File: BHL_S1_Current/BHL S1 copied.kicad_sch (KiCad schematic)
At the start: 96 parts, among them J1 Conn_01x03_Pin, J2 Conn_01x03_Pin, Q1 CSD19502Q5B, Q2 CSD19502Q5B, Q3 CSD19502Q5B, Q4 CSD19502Q5B, Q5 CSD19502Q5B, Q6 CSD19502Q5B, SW1 SW_Push, U1 ME6211C30M5, U2 SPX3819M5-L-5-0, U3 Solder Pad, U4 STM32G431CBUx, Y2 8MHz

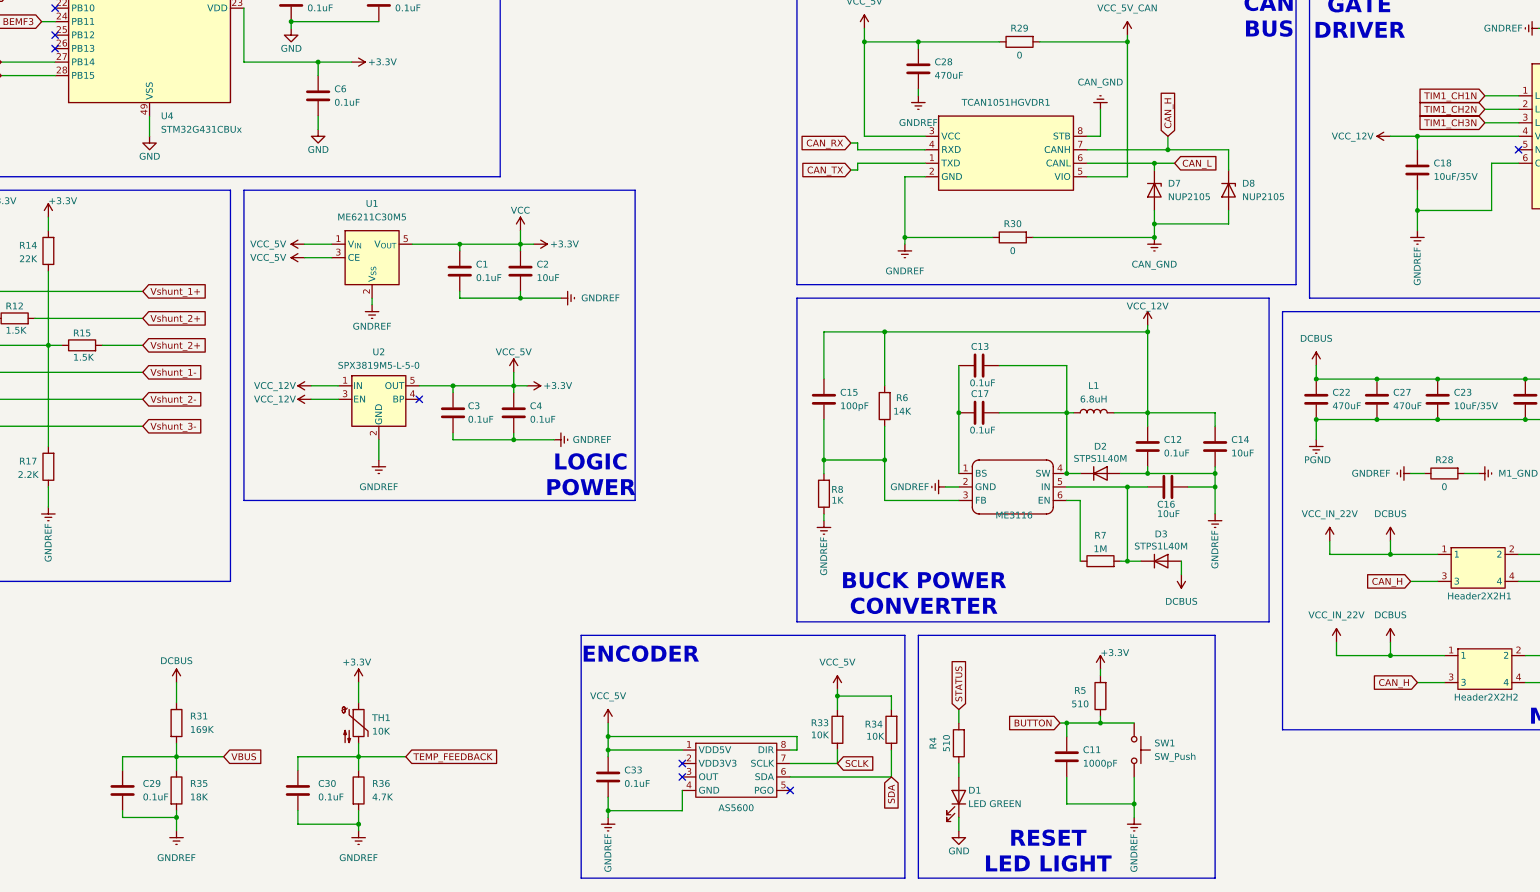
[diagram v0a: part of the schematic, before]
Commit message: Cleanup, Organization, and some edits
Editing the schematic and the PCB. Fixed a lot of ERC errors. Organized the mess that it originally was.
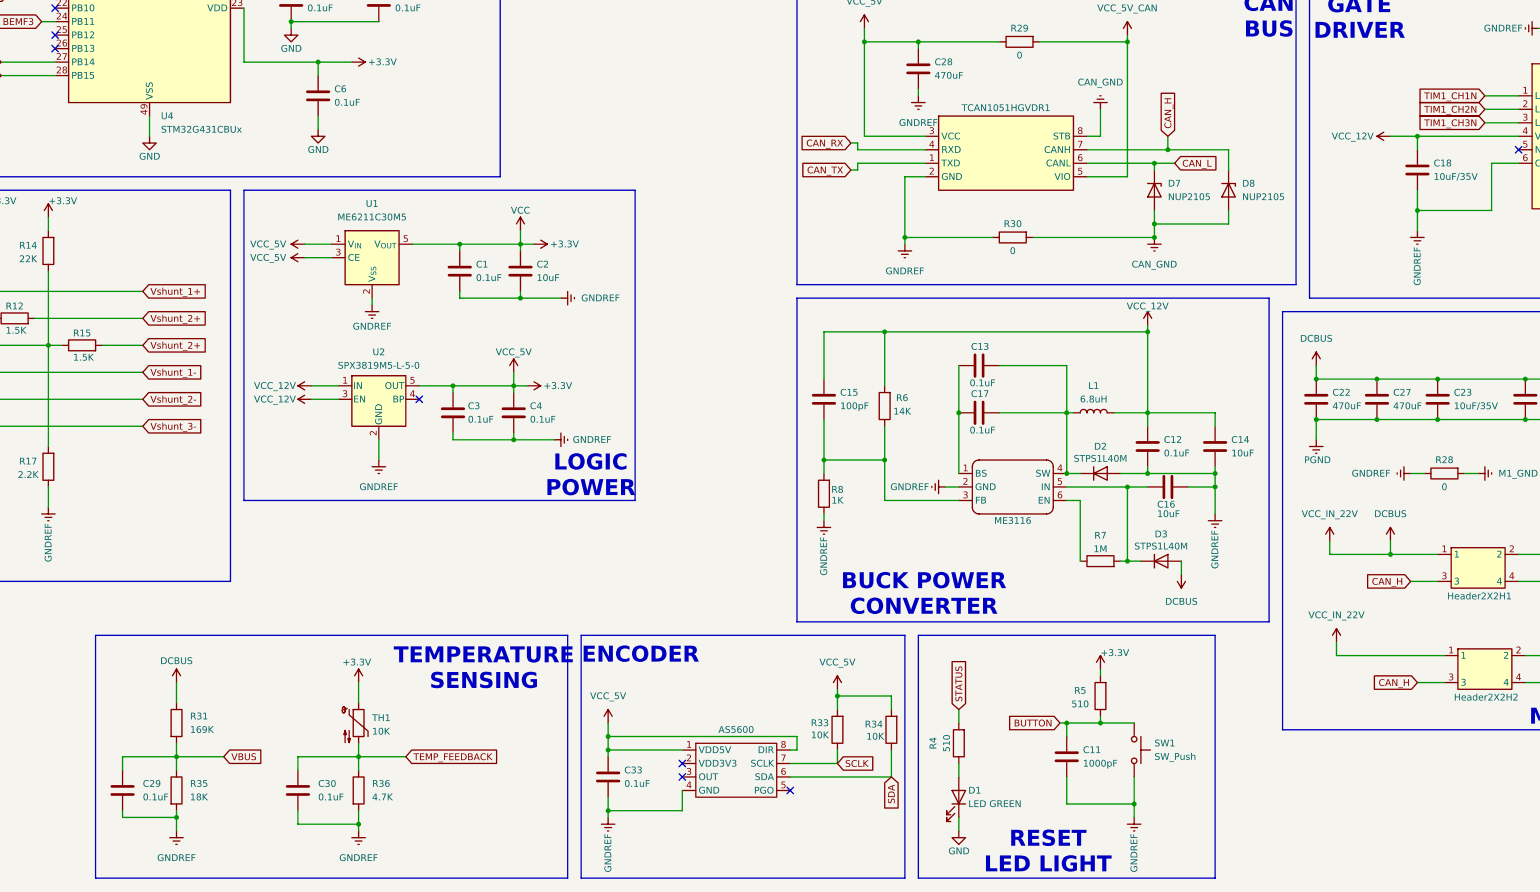
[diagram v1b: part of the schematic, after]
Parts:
- AS5600: symbol Buck converter:AS5600 -> BHL_S1_Components:AS5600
- Header2X2H1, Header2X2H2: symbol Buck converter:Header_2X2H -> BHL_S1_Components:Header_2X2H
- IR2136STRPBF1: symbol Buck converter:IR2136STRPBF -> BHL_S1_Components:IR2136STRPBF
- ME3116: symbol Buck converter:ME3116 -> BHL_S1_Components:ME3116
- TCAN1051HGVDR1: symbol Buck converter:TCAN1051HGVDR -> BHL_S1_Components:TCAN1051HGVDR
- U3: symbol Buck converter:SOLDERPAD_BLDC -> BHL_S1_Components:SOLDERPAD_BLDC
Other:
- note added: "TEMPERATURE SENSING"
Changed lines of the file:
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@@
 	)
 	(rectangle
+		(start 86.36 233.68)
+		(end 175.26 279.4)
+		(stroke
+			(width 0)
+			(type default)
+		)
+		(fill
+			(type none)
+		)
+	)
+	(rectangle
 		(start 241.3 233.68)
 		(end 297.18 279.4)
@@
 		)
 	)
+	(text "TEMPERATURE \nSENSING"
+		(exclude_from_sim no)
+		(at 159.512 240.03 0)
+		(effects
+			(font
+				(face "KiCad Font")
+				(size 3 3)
+				(thickness 2)
+				(bold yes)
+				(color 194 0 0 1)
+			)
+		)
+	)
 	(text "LOGIC\nPOWER\n"
 		(exclude_from_sim no)
@@
 	)
 	(junction
-		(at 330.2 237.49)
-		(diameter 0)
-		(color 0 0 0 0)
-	)
-	(junction
 		(at 223.52 200.66)
 		(diameter 0)
@@
 	(wire
 		(pts
-			(xy 330.2 234.95) (xy 330.2 237.49)
-		)
-		(stroke
-			(width 0)
-			(type default)
-		)
-	)
-	(wire
-		(pts
 			(xy 361.95 88.9) (xy 364.49 88.9)
 		)
@@
 	(wire
 		(pts
-			(xy 340.36 237.49) (xy 330.2 237.49)
+			(xy 320.04 237.49) (xy 340.36 237.49)
 		)
 		(stroke
@@
 	(wire
 		(pts
-			(xy 330.2 237.49) (xy 320.04 237.49)
-		)
-		(stroke
-			(width 0)
-			(type default)
-		)
-	)
-	(wire
-		(pts
 			(xy 375.92 99.06) (xy 375.92 104.14)
 		)
@@
 	)
 	(symbol
-		(lib_id "Buck converter:Header_2X2H")
+		(lib_id "BHL_S1_Components:Header_2X2H")
 		(at 347.98 240.03 0)
 		(unit 1)
@@
 	)
 	(symbol
+		(lib_name "VCC_1")
 		(lib_id "power:VCC")
 		(at 127 186.69 90)
@@
 	)
 	(symbol
-		(lib_id "Buck converter:IR2136STRPBF")
+		(lib_id "BHL_S1_Components:IR2136STRPBF")
 		(at 370.84 139.7 0)
 		(unit 1)
@@
 	)
 	(symbol
-		(lib_id "Buck converter:ME3116")
+		(lib_id "BHL_S1_Components:ME3116")
 		(at 259.08 205.74 0)
 		(unit 1)
@@
 		(dnp no)
 		(property "Reference" "ME3116"
-			(at 259.334 211.074 0)
+			(at 259.08 212.09 0)
 			(effects
 				(font
@@
 	)
 	(symbol
-		(lib_id "Buck converter:SOLDERPAD_BLDC")
+		(lib_id "BHL_S1_Components:SOLDERPAD_BLDC")
 		(at 389.89 52.07 0)
 		(unit 1)
@@
 	)
 	(symbol
-		(lib_id "power:VBUS")
-		(at 330.2 234.95 0)
-		(unit 1)
-		(exclude_from_sim no)
-		(in_bom yes)
-		(on_board yes)
-		(dnp no)
-		(fields_autoplaced yes)
-		(property "Reference" "#PWR067"
-			(at 330.2 238.76 0)
-			(effects
-				(font
-					(size 1.27 1.27)
-				)
-				(hide yes)
-			)
-		)
-		(property "Value" "DCBUS"
-			(at 330.2 229.87 0)
-			(effects
-				(font
-					(size 1.27 1.27)
-				)
-			)
-		)
-		(property "Footprint" ""
-			(at 330.2 234.95 0)
-			(effects
-				(font
-					(size 1.27 1.27)
-				)
-				(hide yes)
-			)
-		)
-		(property "Datasheet" ""
-			(at 330.2 234.95 0)
-			(effects
-				(font
-					(size 1.27 1.27)
-				)
-				(hide yes)
-			)
-		)
-		(property "Description" "Power symbol creates a global label with name \"VBUS\""
-			(at 330.2 234.95 0)
-			(effects
-				(font
-					(size 1.27 1.27)
-				)
-				(hide yes)
-			)
-		)
-		(pin "1"
-		)
-		(instances
-			(project "BHL S1 copied"
-				(path "/0363b2da-c10c-4051-b2e0-f0863b63e8b4"
-					(reference "#PWR067")
-					(unit 1)
-				)
-			)
-		)
-	)
-	(symbol
 		(lib_id "Diode:ESD5Zxx")
 		(at 299.72 149.86 270)
@@
 	)
 	(symbol
-		(lib_id "Buck converter:TCAN1051HGVDR")
+		(lib_id "BHL_S1_Components:TCAN1051HGVDR")
 		(at 257.81 143.51 0)
 		(unit 1)
@@
 		(on_board yes)
 		(dnp no)
-		(fields_autoplaced yes)
 		(property "Reference" "TCAN1051HGVDR1"
-			(at 257.81 133.35 0)
+			(at 257.81 134.366 0)
 			(effects
 				(font
@@
 	)
 	(symbol
-		(lib_id "Buck converter:Header_2X2H")
+		(lib_id "BHL_S1_Components:Header_2X2H")
 		(at 346.71 220.98 0)
 		(unit 1)
@@
 	)
 	(symbol
-		(lib_id "Buck converter:AS5600")
+		(lib_id "BHL_S1_Components:AS5600")
 		(at 207.01 259.08 0)
 		(unit 1)
@@
 		(fields_autoplaced yes)
 		(property "Reference" "AS5600"
-			(at 207.01 266.192 0)
+			(at 207.01 251.46 0)
 			(effects
 				(font

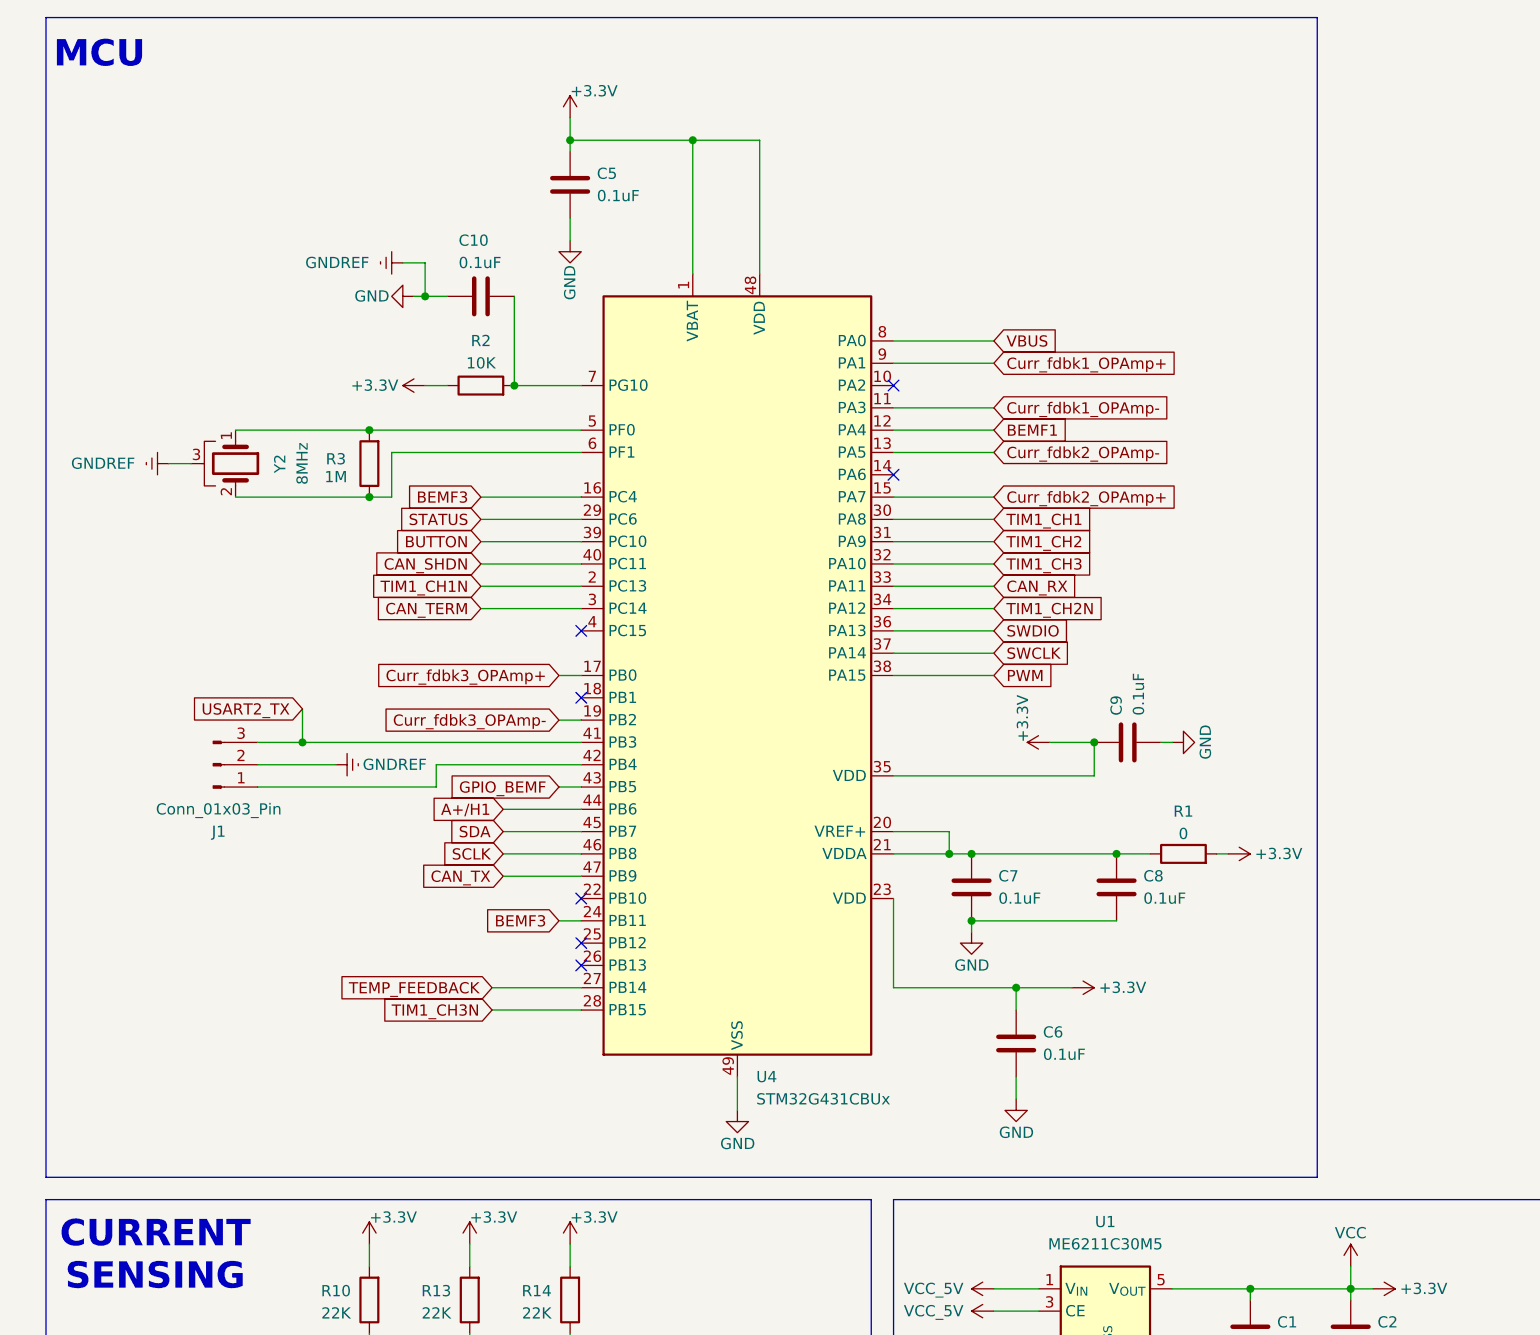
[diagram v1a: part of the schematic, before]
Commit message: Organization along with more edits to schematic
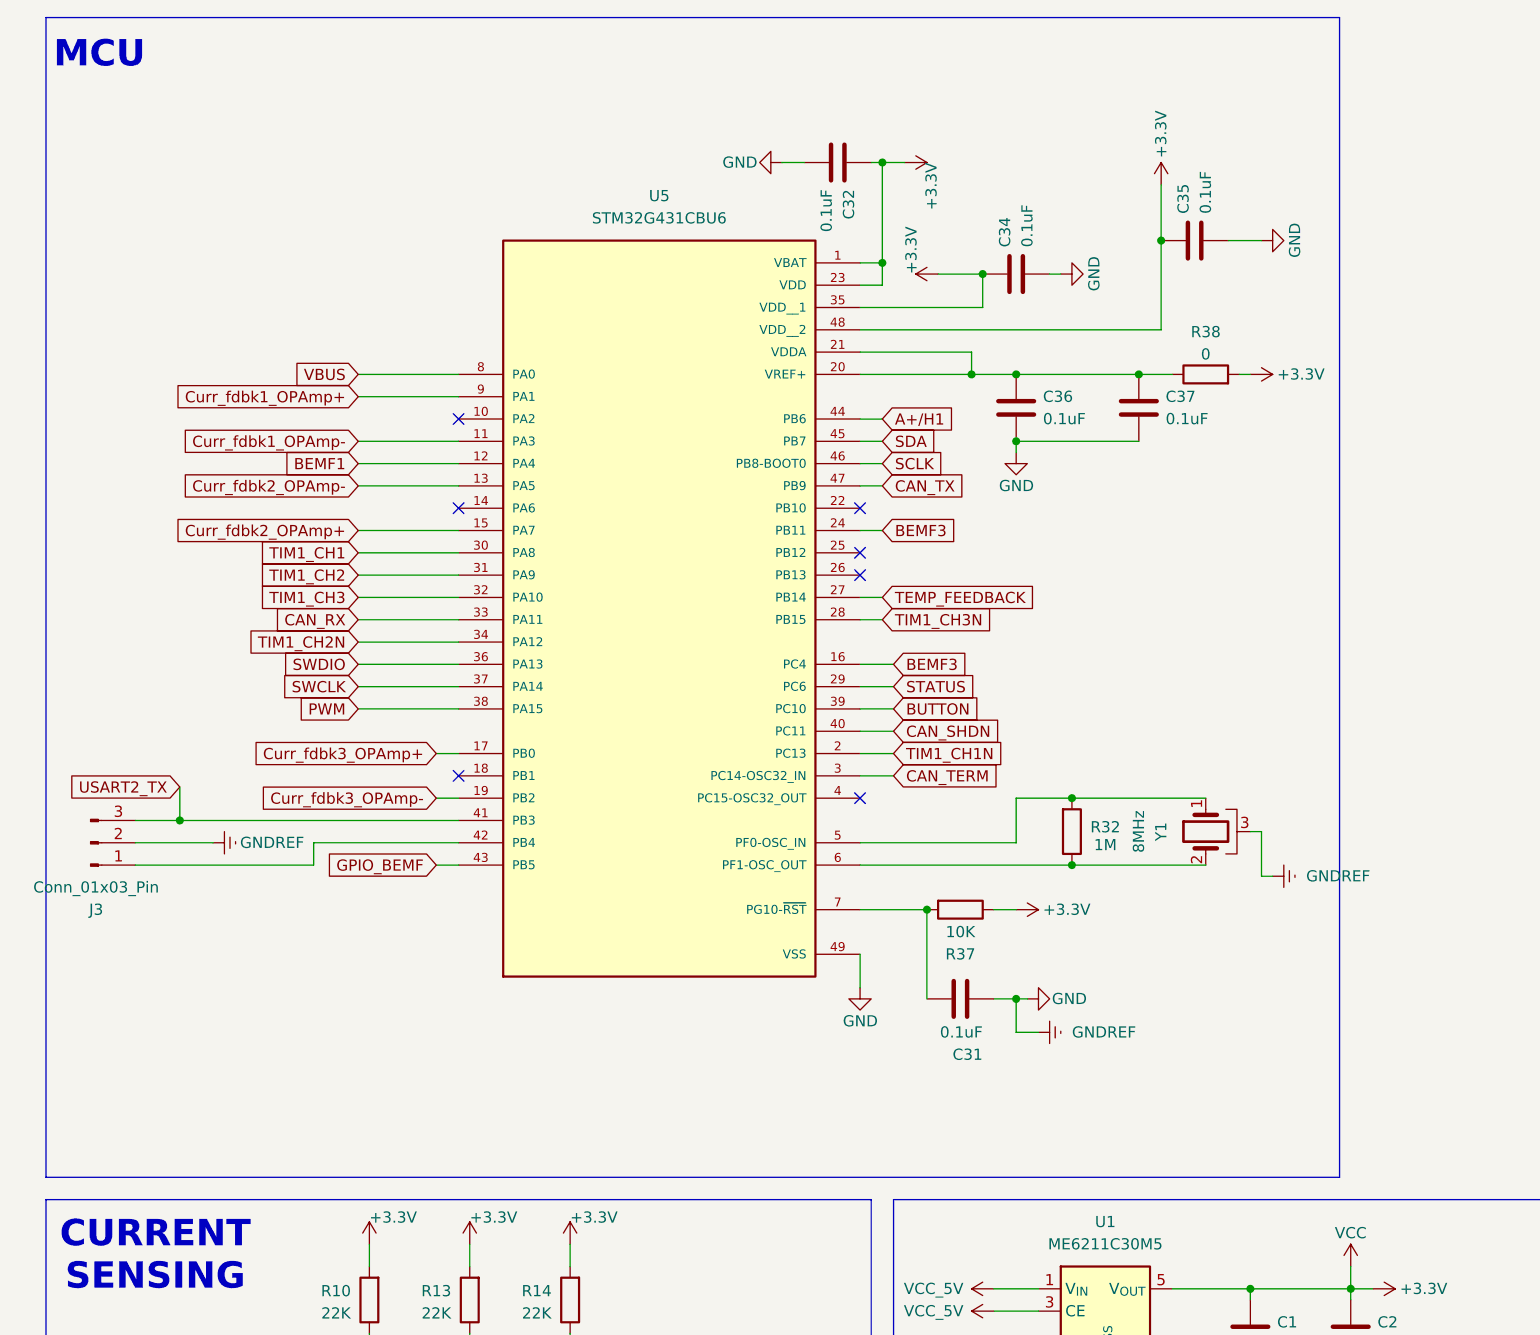
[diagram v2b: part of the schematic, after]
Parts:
- removed C10, C5, C6, C7, C8, C9: 0.1uF, Capacitor_SMD:C_0402_1005Metric_Pad0.74x0.62mm_HandSolder, symbol Device:C
- removed J1: Conn_01x03_Pin, Connector_PinHeader_2.54mm:PinHeader_1x03_P2.54mm_Vertical, symbol Connector:Conn_01x03_Pin
- removed R1: 0, Resistor_SMD:R_01005_0402Metric_Pad0.57x0.30mm_HandSolder, symbol Device:R
- removed R2: 10K, Resistor_SMD:R_01005_0402Metric_Pad0.57x0.30mm_HandSolder, symbol Device:R
- removed R3: 1M, Resistor_SMD:R_0603_1608Metric_Pad0.98x0.95mm_HandSolder, symbol Device:R
- removed U4: STM32G431CBUx, Package_DFN_QFN:QFN-44-1EP_7x7mm_P0.5mm_EP5.2x5.2mm, symbol MCU_ST_STM32G4:STM32G431CBUx
- removed Y2: 8MHz, Footprint for BHL S1:ABM8AAIG8000MHzV2RT3_Crystal, symbol Device:Crystal_GND3
- added C31, C32, C34, C35, C36, C37: 0.1uF, Capacitor_SMD:C_0402_1005Metric_Pad0.74x0.62mm_HandSolder, symbol Device:C
- added J3: Conn_01x03_Pin, Connector_PinHeader_2.54mm:PinHeader_1x03_P2.54mm_Vertical, symbol Connector:Conn_01x03_Pin
- added R32: 1M, Resistor_SMD:R_0603_1608Metric_Pad0.98x0.95mm_HandSolder, symbol Device:R
- added R37: 10K, Resistor_SMD:R_01005_0402Metric_Pad0.57x0.30mm_HandSolder, symbol Device:R
- added R38: 0, Resistor_SMD:R_01005_0402Metric_Pad0.57x0.30mm_HandSolder, symbol Device:R
- added U5: STM32G431CBU6, Footprints:QFN50P700X700X60-49N, symbol BHL_S1_Components:STM32G431CBU6
- added Y1: 8MHz, Footprint for BHL S1:ABM8AAIG8000MHzV2RT3_Crystal, symbol Device:Crystal_GND3
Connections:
- net +3.3V: now also C32.1, C34.1, C35.1, R37.1, R38.2, U5.1 (VBAT), U5.23 (VDD), U5.35 (VDD__1), U5.48 (VDD__2)
- net A+/H1: now also U5.44 (PB6)
- net BEMF1: now also U5.12 (PA4)
- net BEMF3: now also U5.16 (PC4), U5.24 (PB11)
- net BUTTON: now also U5.39 (PC10)
- net CAN_RX: now also U5.33 (PA11)
- net CAN_SHDN: now also U5.40 (PC11)
- net CAN_TERM: now also U5.3 (PC14-OSC32_IN)
- net CAN_TX: now also U5.47 (PB9)
- net Curr_fdbk1_OPAmp+: now also U5.9 (PA1)
- net Curr_fdbk2_OPAmp+: now also U5.15 (PA7)
- net Curr_fdbk3_OPAmp+: now also U5.17 (PB0)
- net GND: now also C31.1, C32.2, C34.2, C35.2, C36.2, C37.2, J3.2 (Pin_2), U5.49 (VSS), Y1.3
- net GPIO_BEMF: now also U5.43 (PB5)
- net PGND: now also U5.11 (PA3), U5.13 (PA5), U5.19 (PB2)
- net PWM: now also U5.38 (PA15)
- net SCLK: now also U5.46 (PB8-BOOT0)
- net SDA: now also U5.45 (PB7)
- net STATUS: now also U5.29 (PC6)
- net SWCLK: now also U5.37 (PA14)
- net SWDIO: now also U5.36 (PA13)
- net TEMP_FEEDBACK: now also U5.27 (PB14)
- net TIM1_CH1: now also U5.30 (PA8)
- net TIM1_CH1N: now also U5.2 (PC13)
- net TIM1_CH2: now also U5.31 (PA9)
- net TIM1_CH2N: now also U5.34 (PA12)
- net TIM1_CH3: now also U5.32 (PA10)
- net TIM1_CH3N: now also U5.28 (PB15)
- net USART2_TX: now also J3.3 (Pin_3), U5.41 (PB3)
- net VBUS: now also U5.8 (PA0)
- new net: C36.1, C37.1, R38.1, U5.20 (VREF+), U5.21 (VDDA)
- new net: C31.2, R37.2, U5.7 (PG10-~{RST})
- new net: J3.1 (Pin_1), U5.42 (PB4)
- new net: R32.2, U5.5 (PF0-OSC_IN), Y1.1
- new net: R32.1, U5.6 (PF1-OSC_OUT), Y1.2
